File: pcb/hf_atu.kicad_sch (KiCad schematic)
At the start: 119 parts, among them J10 To CTRL:ATU, J11 TO TX_FILT_OUT, J12 TO SWR_IN, J8 SWR_IN, J9 SWR_OUT, K14 G6E, K15 G6E, K16 G6E, K17 G6E, K18 G6E, K19 G6E, K20 G6E, K21 G6E, K22 G6E, K23 G6E, K24 G6E, K25 G6E, K26 G6E, K27 G6E, K28 G6E, K29 G6E, K30 G6E, T1 SWR, U4 MCP23017_SO, U5 ULN2803A, U6 ULN2803A, U7 MCP23008-xSO, U8 ULN2803A

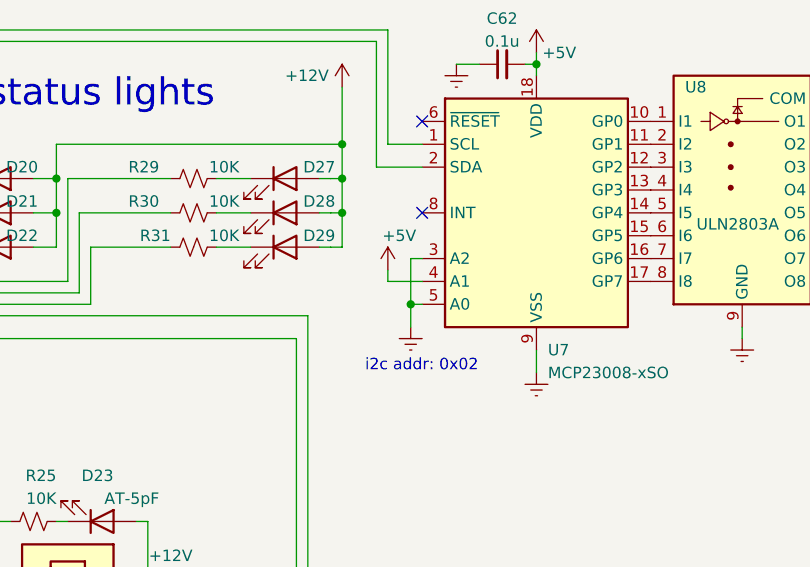
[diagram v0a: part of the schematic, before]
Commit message: update to gpiod v2 api; fix typo in logger; fix issue with atu i2c address line short
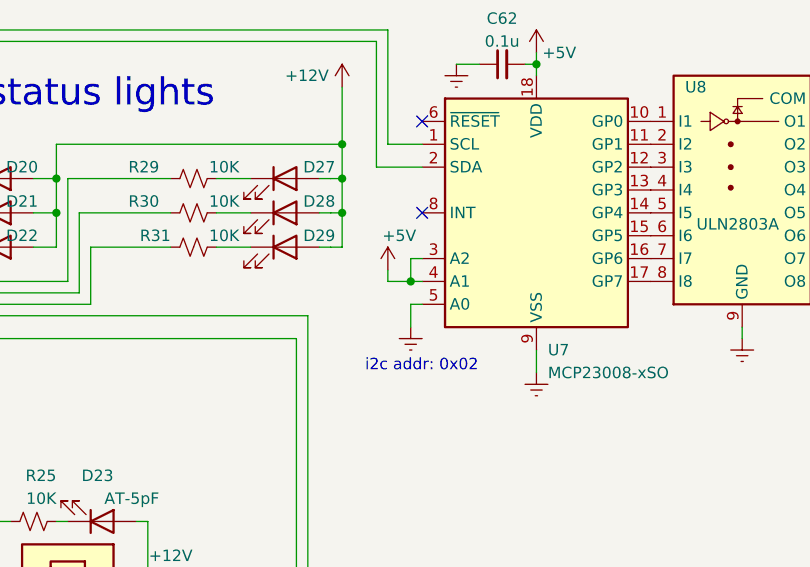
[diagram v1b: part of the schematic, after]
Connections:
- net +5V: now also U7.3 (A2)
- net Earth: no longer U7.3 (A2)
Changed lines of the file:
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@@
 	(title_block
 		(title "HF Antenna Matching Unit")
-		(rev "2023/08/24")
+		(rev "2025/01/30")
 	)
 	(junction
@@
 	)
 	(junction
+		(at 175.26 41.91)
+		(diameter 0)
+		(color 0 0 0 0)
+	)
+	(junction
 		(at 167.64 26.67)
 		(diameter 0)
@@
 	)
 	(junction
-		(at 175.26 44.45)
-		(diameter 0)
-		(color 0 0 0 0)
-	)
-	(junction
 		(at 110.49 140.97)
 		(diameter 0)
@@
 	(wire
 		(pts
+			(xy 175.26 39.37) (xy 175.26 41.91)
+		)
+		(stroke
+			(width 0)
+			(type default)
+		)
+	)
+	(wire
+		(pts
 			(xy 24.13 140.97) (xy 24.13 130.81)
 		)
@@
 	(wire
 		(pts
-			(xy 172.72 41.91) (xy 176.53 41.91)
+			(xy 172.72 41.91) (xy 175.26 41.91)
 		)
 		(stroke
@@
 	(wire
 		(pts
-			(xy 175.26 39.37) (xy 175.26 44.45)
-		)
-		(stroke
-			(width 0)
-			(type default)
-		)
-	)
-	(wire
-		(pts
 			(xy 233.68 138.43) (xy 234.95 138.43)
 		)
@@
 		)
 	)
+	(wire
+		(pts
+			(xy 175.26 41.91) (xy 176.53 41.91)
+		)
+		(stroke
+			(width 0)
+			(type default)
+		)
+	)
